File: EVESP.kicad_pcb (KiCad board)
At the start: 2 copper layers, 106 parts, among them J1 Screw_Terminal_01x08, J2 Screw_Terminal_01x06, J3 Conn_01x04, J4 Conn_01x16_Male, J5 Conn_01x16_Female, J6 Conn_01x20_Female, J7 Conn_01x20_Male, J8 Screw_Terminal_01x03, J9 Screw_Terminal_01x03, Q1 BC847, Q2 BC847, Q3 BC847, U1 LM7332, U2 MOC3063M, U3 MOC3063M, U4 MOC3063M, U5 LM7332

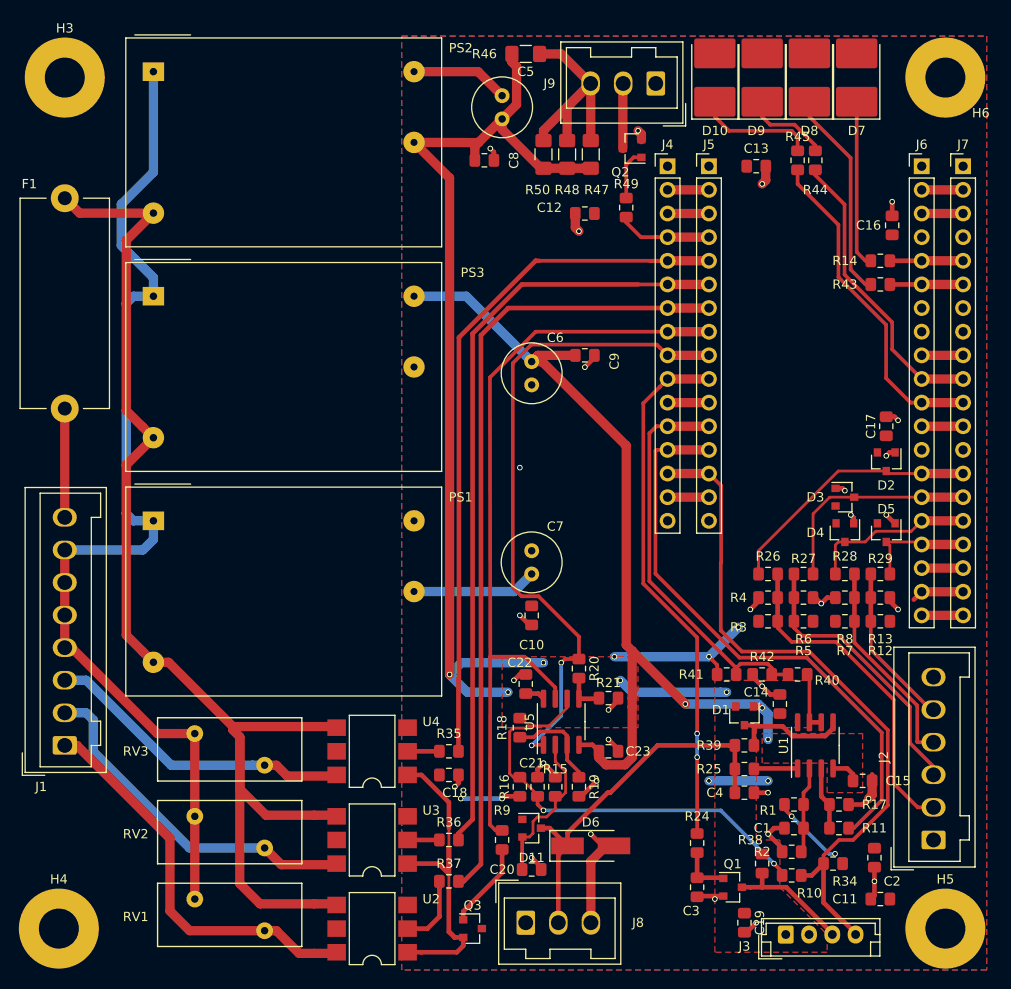
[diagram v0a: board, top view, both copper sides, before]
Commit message: Layout shrink to <= 10cm x 10 cm
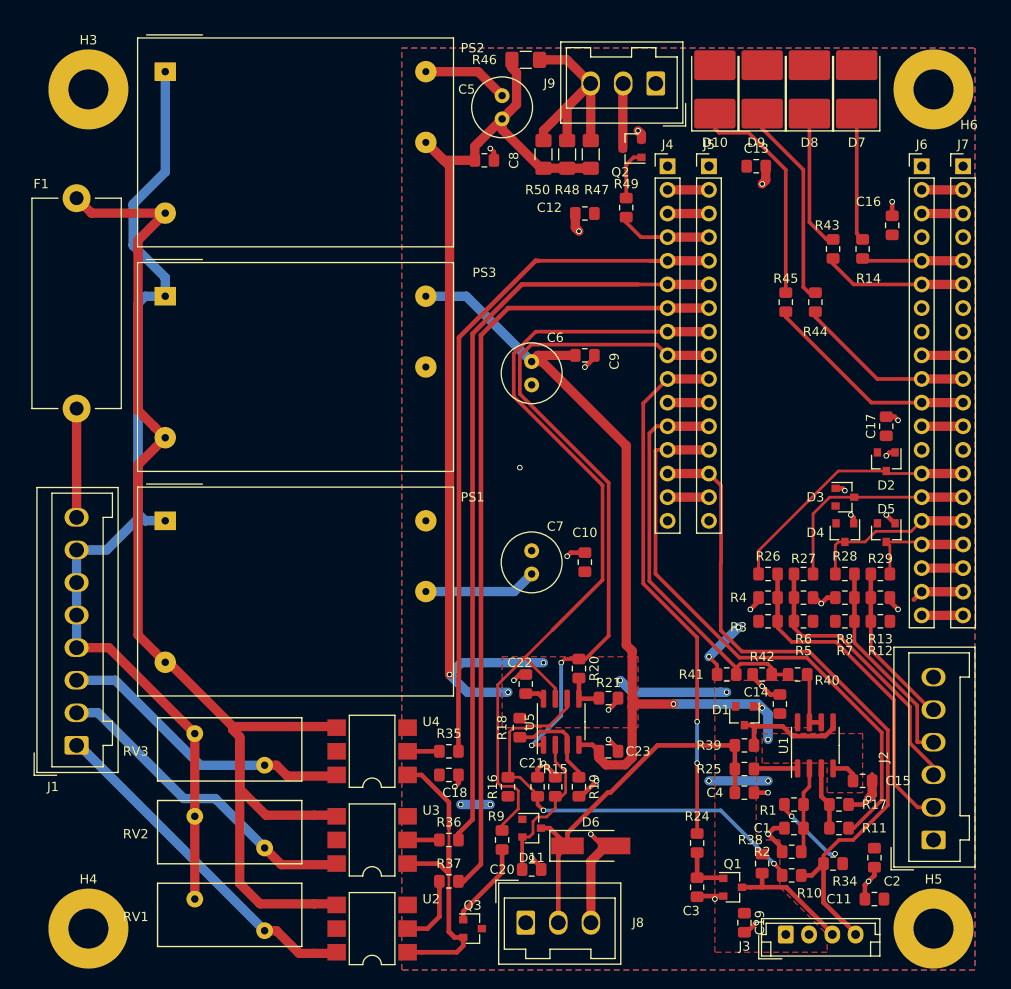
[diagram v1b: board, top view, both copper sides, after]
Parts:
- moved R45 15.3 mm to (124.5, 91.4)
- moved R44 15.2 mm to (127.6, 91.4)
- moved C10 8.08 mm to (102.9, 119.4), turned to 90 degrees
- moved R43 6.35 mm to (129.5, 85.7), turned to 270 degrees
- moved H4 3.18 mm to (49.5, 158.8)
- moved H3 2.84 mm to (49.5, 68.6)
- moved R14 2.29 mm to (132.7, 85.7), turned to 270 degrees
- moved H6 1.80 mm to (140.3, 68.6)
- moved R16 1.27 mm to (94.6, 143.5)
- moved D10 1.27 mm to (116.8, 68.6)
- moved D7 1.27 mm to (132.1, 68.6)
- moved D8 1.27 mm to (127.0, 68.6)
- moved D9 1.27 mm to (121.9, 68.6)
- moved F1 1.27 mm to (48.3, 102.9)
- moved J1 1.27 mm to (48.3, 139.1)
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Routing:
- net +3V3: track 51.1 -> 36.4 mm, vias 10 -> 9
- net Net-(D10-Pad1): track 12.9 -> 25.9 mm
- net Net-(D9-Pad1): track 9.17 -> 22.0 mm
- net /LED1_n: track 31.6 -> 19.2 mm
- net /LED0_n: track 39.6 -> 27.3 mm
- net Net-(D8-Pad1): track 22.7 -> 16.6 mm
- net /REL_0: track 43.0 -> 37.2 mm
- net /SafeToCharge: track 84.7 -> 90.0 mm
- net /N: track 114.1 -> 109.4 mm
- net -12V: track 99.8 -> 96.3 mm
- net /REL_1: track 38.3 -> 35.0 mm
- net /LED2_n: track 12.3 -> 15.5 mm
- net Net-(D7-Pad1): track 18.0 -> 15.4 mm
- net +12V: track 123.4 -> 121.4 mm
- net /L1_fused: track 131.5 -> 129.9 mm
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
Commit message: Added edge prints. Added prints.
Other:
- board outline added: 99.7 x 99.1 mm
- board text added: "EVESP v1.0 Bottom"
- board text added: "EVESP v1.0 Top"
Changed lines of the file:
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@@
   (general
     (thickness 1.6)
-    (drawings 0)
+    (drawings 8)
     (tracks 611)
     (zones 0)
@@
     (0 F.Cu signal)
     (31 B.Cu signal)
-    (32 B.Adhes user)
-    (33 F.Adhes user)
-    (34 B.Paste user)
-    (35 F.Paste user)
+    (32 B.Adhes user hide)
+    (33 F.Adhes user hide)
+    (34 B.Paste user hide)
+    (35 F.Paste user hide)
     (36 B.SilkS user)
     (37 F.SilkS user)
@@
     (46 B.CrtYd user)
     (47 F.CrtYd user)
-    (48 B.Fab user)
-    (49 F.Fab user)
+    (48 B.Fab user hide)
+    (49 F.Fab user hide)
   )
   (setup
@@
     )
   )
+  (gr_text "EVESP v1.0\nBottom" (at 124.46 69.215) (layer B.Cu)
+    (effects (font (size 1.5 1.5) (thickness 0.3)) (justify mirror))
+  )
+  (gr_text "EVESP v1.0\nTop" (at 94.615 83.82) (layer F.Cu)
+    (effects (font (size 1 1) (thickness 0.2)))
+  )
+  (gr_text "EVESP v1.0\nBottom" (at 98.425 111.125) (layer B.SilkS)
+    (effects (font (size 1 1) (thickness 0.15)) (justify mirror))
+  )
+  (gr_text "EVESP v1.0\nTop" (at 99.06 107.315) (layer F.SilkS)
+    (effects (font (size 2 2) (thickness 0.15)))
+  )
+  (gr_line (start 45.085 163.195) (end 144.78 163.195) (layer Edge.Cuts) (width 0.1))
+  (gr_line (start 45.085 64.135) (end 45.085 163.195) (layer Edge.Cuts) (width 0.1))
+  (gr_line (start 144.78 64.135) (end 45.085 64.135) (layer Edge.Cuts) (width 0.1))
+  (gr_line (start 144.78 163.195) (end 144.78 64.135) (layer Edge.Cuts) (width 0.1))
   (via (at 92.71 145.415) (size 0.6) (drill 0.4) (layers F.Cu B.Cu) (net 2))
   (via (at 89.535 145.415) (size 0.6) (drill 0.4) (layers F.Cu B.Cu) (net 2))

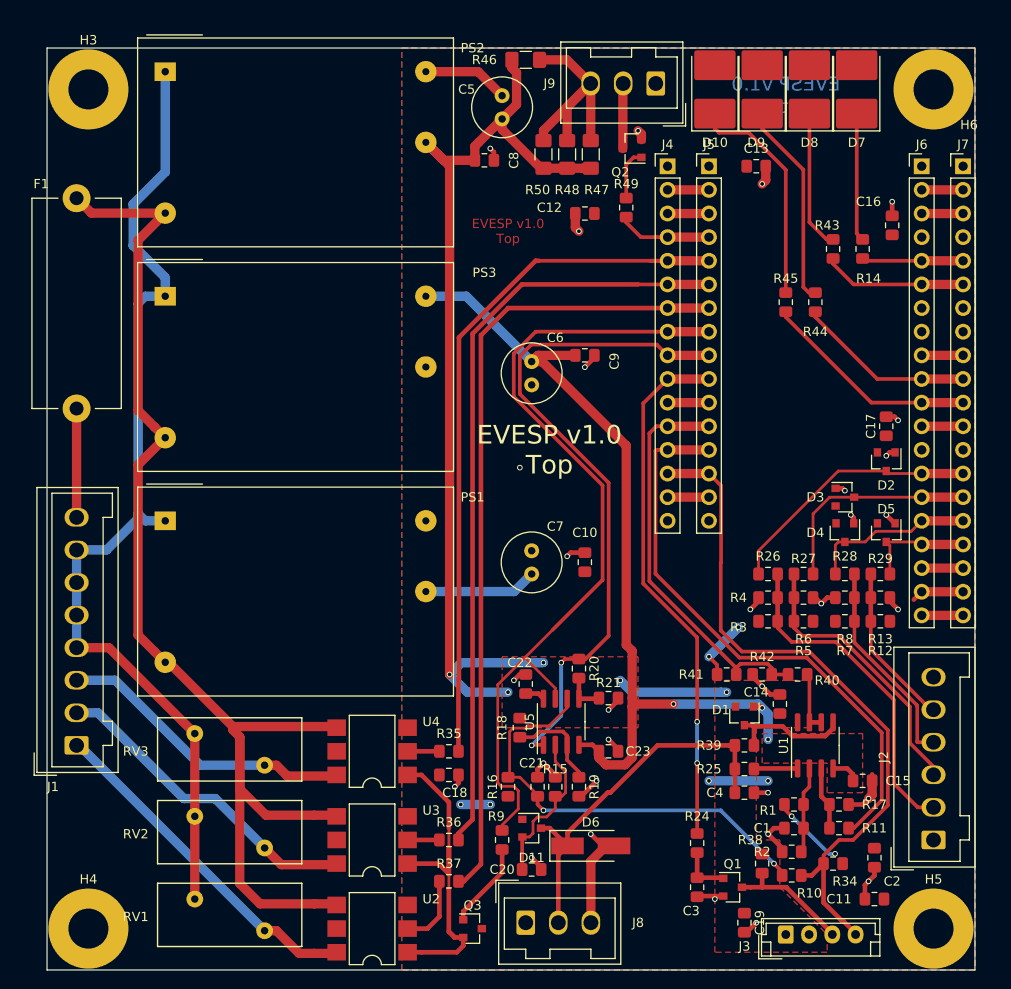
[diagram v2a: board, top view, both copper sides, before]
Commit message: Better +3V3 plane.
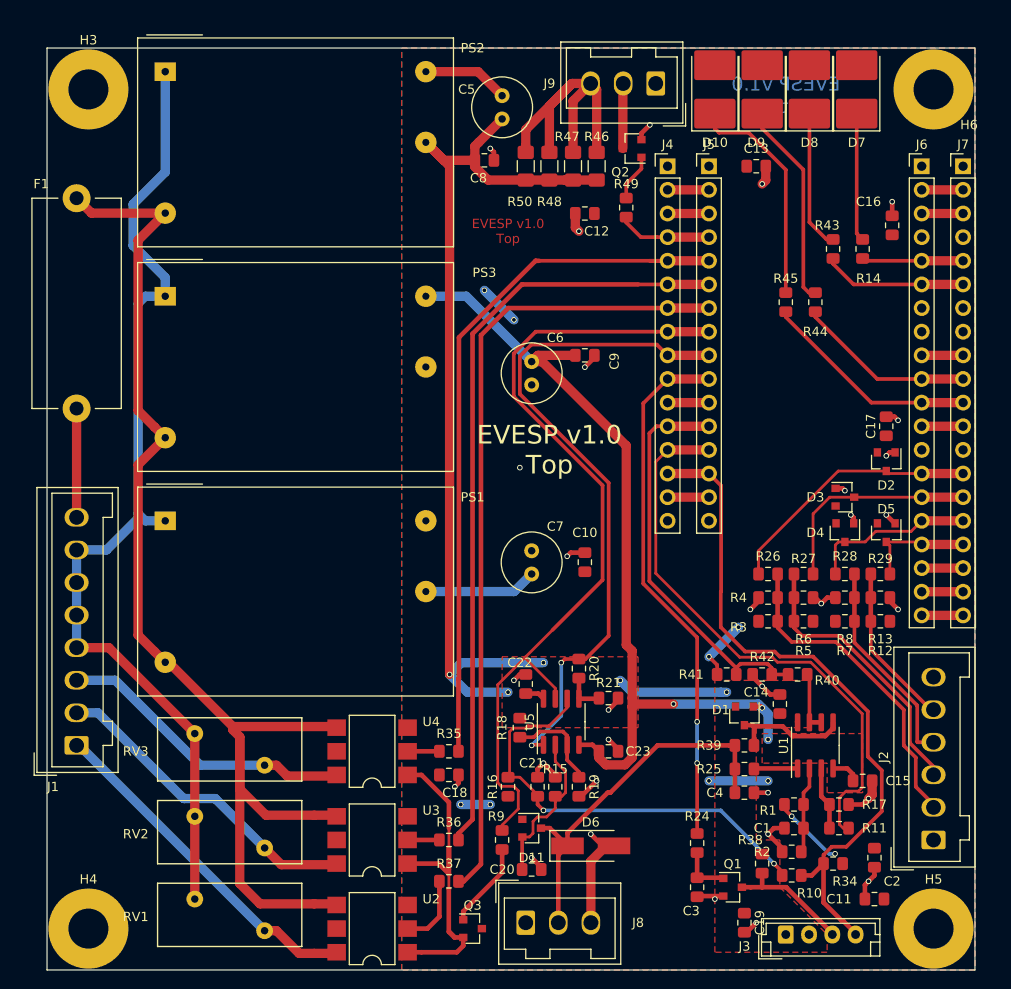
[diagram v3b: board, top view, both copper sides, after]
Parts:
- moved R46 13.7 mm to (104.1, 76.8), turned to 90 degrees
- moved R47 2.29 mm to (101.6, 76.8)
- moved R48 2.29 mm to (99.1, 76.8)
- moved R50 2.29 mm to (96.5, 76.8)
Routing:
- net Net-(J9-Pad3): track 28.1 -> 35.7 mm
- net +12V: track 121.4 -> 116.5 mm
- net +3V3: track 36.4 -> 40.8 mm, vias 9 -> 11
- net Net-(J6-Pad19): track 5.65 -> 4.44 mm
- net Net-(J2-Pad2): track 35.8 -> 34.8 mm
- net /CP_out: track 62.5 -> 61.5 mm
- net /RCM_fail: track 74.4 -> 73.6 mm

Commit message: AC side changed for 2mm clearance.
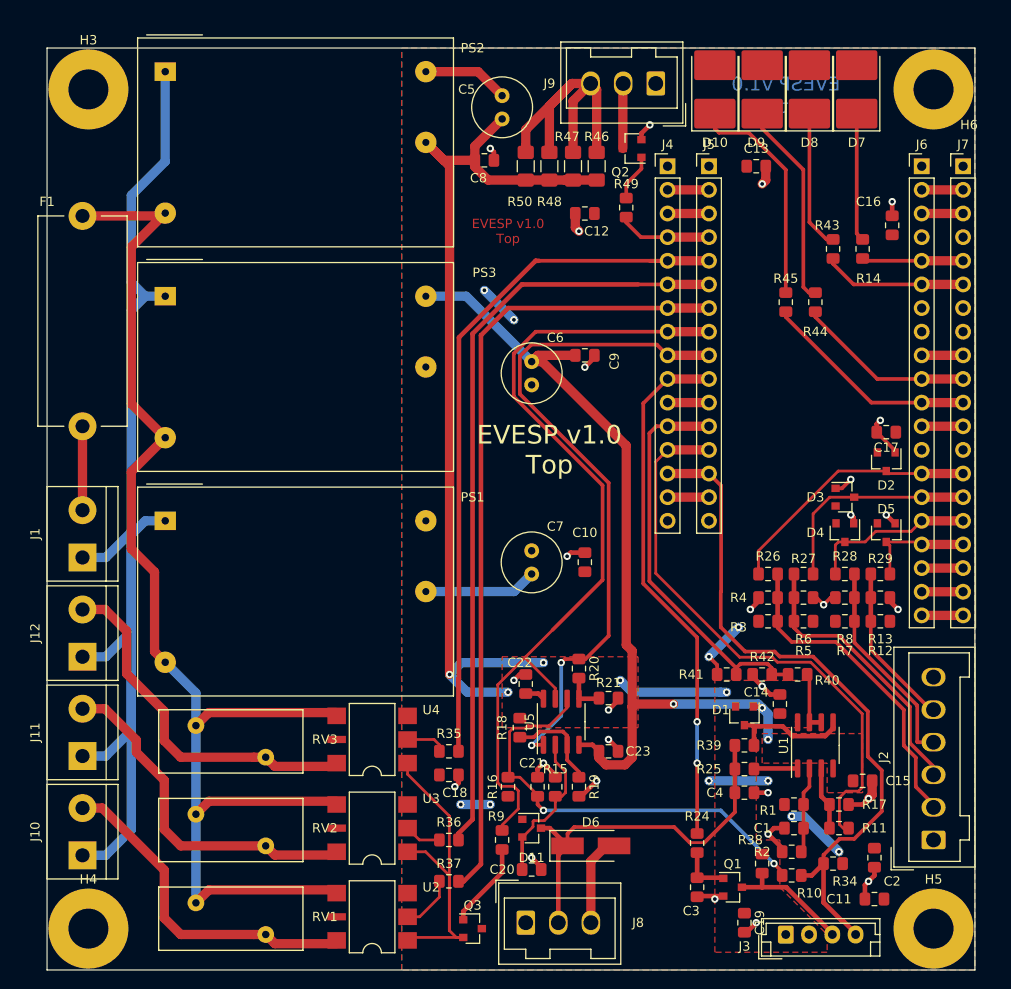
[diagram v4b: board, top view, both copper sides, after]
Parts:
- added J10: Screw_Terminal_01x02, TerminalBlock:TerminalBlock_bornier-2_P5.08mm, F.Cu at (48.9, 150.9)
- added J11: Screw_Terminal_01x02, TerminalBlock:TerminalBlock_bornier-2_P5.08mm, F.Cu at (48.9, 140.2)
- added J12: Screw_Terminal_01x02, TerminalBlock:TerminalBlock_bornier-2_P5.08mm, F.Cu at (48.9, 129.5)
- J1: value Screw_Terminal_01x08 -> Screw_Terminal_01x02; footprint Connector_Wago:Wago_734-138_1x08_P3.50mm_Vertical -> TerminalBlock:TerminalBlock_bornier-2_P5.08mm
- moved J1 20.2 mm to (48.9, 118.9)
- moved RV1 8.52 mm to (68.6, 159.4), turned to 180 degrees
- moved RV2 8.26 mm to (68.6, 149.9), turned to 180 degrees
- moved RV3 8.03 mm to (68.6, 140.3), turned to 180 degrees
- moved F1 2.01 mm to (48.9, 104.8)
- moved U2 1.27 mm to (80.0, 157.5)
- moved U3 1.27 mm to (80.0, 148.0)
- moved U4 1.27 mm to (80.0, 138.4)
- moved C17 0.63 mm to (135.3, 105.4), turned to 180 degrees
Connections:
- J1 pad 1: /REL_0 -> /N
- J1 pad 2: /REL_1 -> /L1
- RV1 pad 1: /N -> /REL_0
- RV1 pad 2: /REL_0 -> /L1_fused
- RV2 pad 1: /N -> /REL_1
- RV2 pad 2: /REL_1 -> /L1_fused
- RV3 pad 1: /N -> /REL_2
- RV3 pad 2: /REL_2 -> /L1_fused
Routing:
- net /N: track 109.4 -> 137.2 mm
- net Net-(Q3-Pad2): track 49.6 -> 39.2 mm
- net /L1_fused: track 129.9 -> 137.6 mm
- net /CP: track 40.7 -> 47.8 mm
- net /REL_2: track 32.2 -> 38.8 mm
- net -12V: track 96.3 -> 93.2 mm
- net /REL_1: track 35.0 -> 37.7 mm
- net /L1: track 11.7 -> 9.02 mm
- net Net-(R35-Pad1): track 2.78 -> 4.36 mm
- net +3V3: track 40.8 -> 39.6 mm, vias 11 -> 10
- net Net-(R36-Pad1): track 2.78 -> 3.95 mm
- net Net-(R37-Pad1): track 7.11 -> 5.99 mm
- net /REL_0: track 37.2 -> 36.4 mm
- net GND: track 89.9 -> 89.8 mm, vias 30 -> 28
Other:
- net class 240Vac: clearance 0.508 -> 2; via_dia 0.6 -> 0.8
- net class Default: via_dia 0.6 -> 0.8

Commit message: Added hysteresis to charge -signal. Schematic review changes fixed.
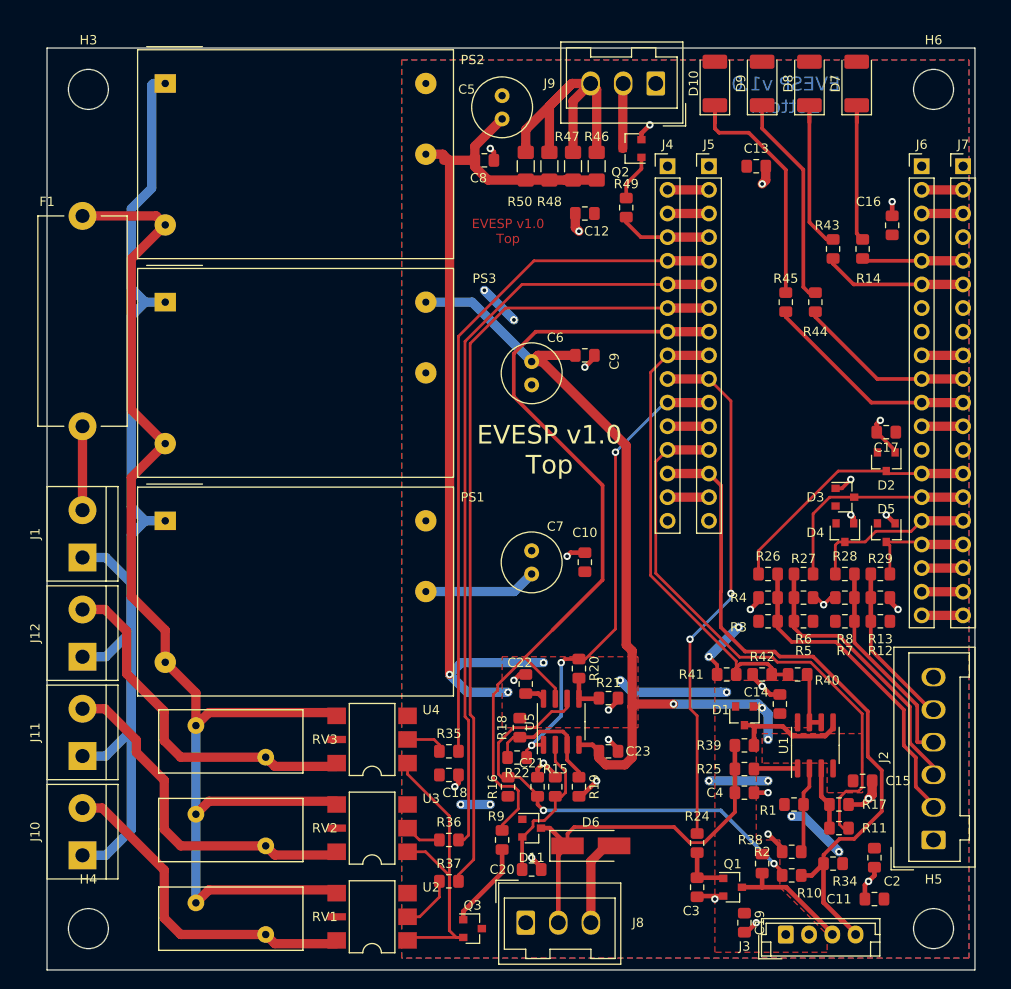
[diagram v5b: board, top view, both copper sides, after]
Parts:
- removed C1: 100n, Resistor_SMD:R_0805_2012Metric_Pad1.15x1.40mm_HandSolder
- added R22: 1M, Resistor_SMD:R_0805_2012Metric_Pad1.15x1.40mm_HandSolder, F.Cu at (95.6, 140.4)
- D10, D7, D8, D9: footprint LED_SMD:LED_2816_7142Metric_Pad3.20x4.45mm_HandSolder -> LED_SMD:LED_2010_5025Metric_Pad1.52x2.65mm_HandSolder
- H3, H4, H5, H6: footprint MountingHole:MountingHole_4.3mm_M4_Pad -> MountingHole:MountingHole_4.3mm_M4
- R2: value DNI 10k -> 10k
- moved PS2 1.27 mm to (57.8, 67.9)
- moved D10 0.64 mm to (116.8, 67.9)
- moved D7 0.64 mm to (132.1, 67.9)
- moved D8 0.64 mm to (127.0, 67.9)
- moved D9 0.64 mm to (121.9, 67.9)
- moved PS3 0.63 mm to (57.8, 91.4)
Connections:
- J4 pad 11: Net-(J4-Pad11) -> /Charge
- J4 pad 12: /CP_in -> Net-(J4-Pad12)
- J4 pad 9: /Charge -> /CP_in
- J5 pad 11: Net-(J4-Pad11) -> /Charge
- J5 pad 12: /CP_in -> Net-(J4-Pad12)
- J5 pad 9: /Charge -> /CP_in
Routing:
- net /Charge: track 73.1 -> 51.6 mm, vias 2 -> 3
- net GND: track 89.8 -> 78.5 mm
- net /CP_in: track 43.1 -> 50.6 mm
- net /N: track 137.2 -> 130.6 mm
- net Net-(J4-Pad12): track 0.00 -> 4.44 mm
- net Net-(J4-Pad11): track 4.44 -> 0.00 mm
- net Net-(R18-Pad2): track 10.5 -> 13.7 mm
- net +12V: track 116.5 -> 113.5 mm
- net /Relay_0_n: track 76.7 -> 74.9 mm
- net Net-(C21-Pad1): track 47.4 -> 49.1 mm
- net /L1_fused: track 137.6 -> 136.6 mm
- net Net-(D9-Pad1): track 22.0 -> 22.9 mm
- net Net-(D8-Pad1): track 16.6 -> 17.5 mm
- net Net-(D7-Pad1): track 15.4 -> 16.2 mm
- net Net-(D10-Pad1): track 25.9 -> 26.7 mm
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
